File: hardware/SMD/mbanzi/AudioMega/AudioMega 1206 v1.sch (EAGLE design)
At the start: 72 parts, among them Q1 BC846ASMD, Q2 BC846ASMD, Q3 BC846ASMD, Q4 2N7002, Q5 BC846ASMD, Q6 BC846ASMD, U1 REG1117-5, U2 REG1117-3.3, U3 ATMEGA328-AU, U4 LM386M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

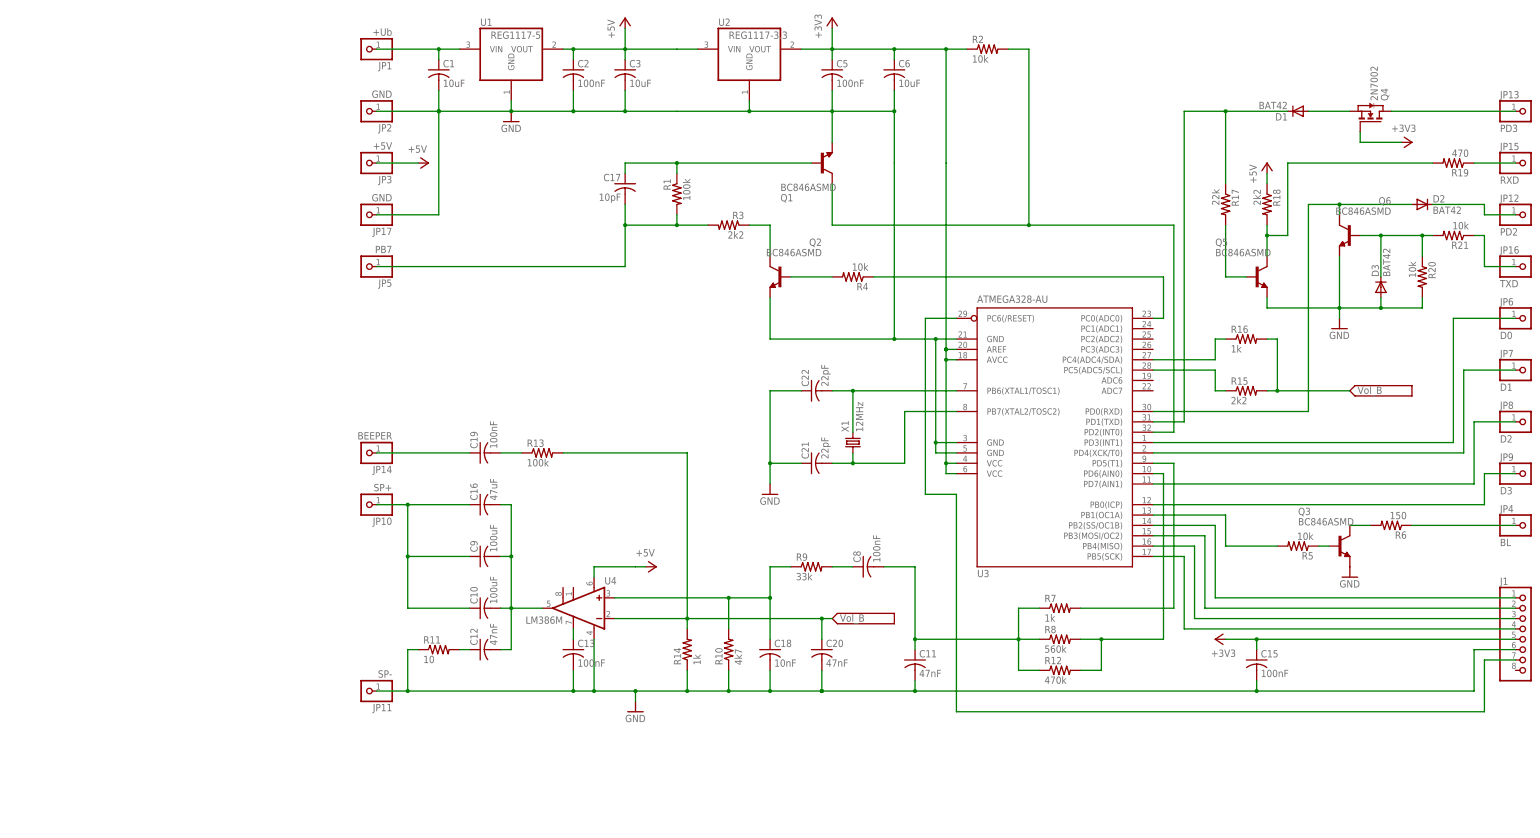
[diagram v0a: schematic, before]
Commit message: Created initial 1206 version of the PCB & renamed files
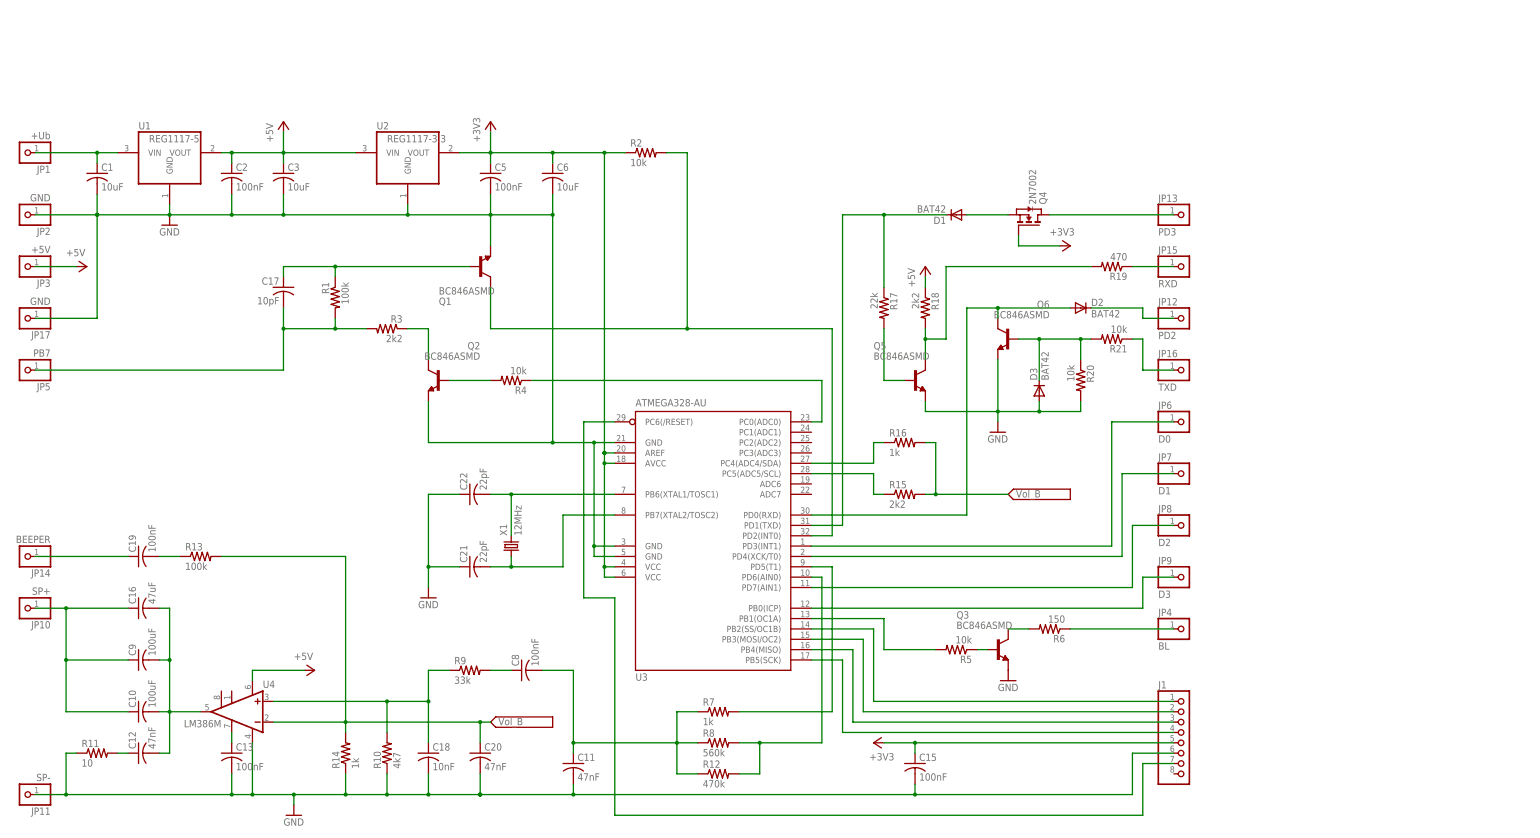
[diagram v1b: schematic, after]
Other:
- moved on the sheet: C1, C10, C11, C12, C13, C15, C16, C17, C18, C19, C2, C20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
